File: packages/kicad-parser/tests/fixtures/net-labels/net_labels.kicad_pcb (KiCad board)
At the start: 4 copper layers, 40 x 40 mm, 2 parts, among them J1 NetLabels_Back, U1 NetLabels_Front

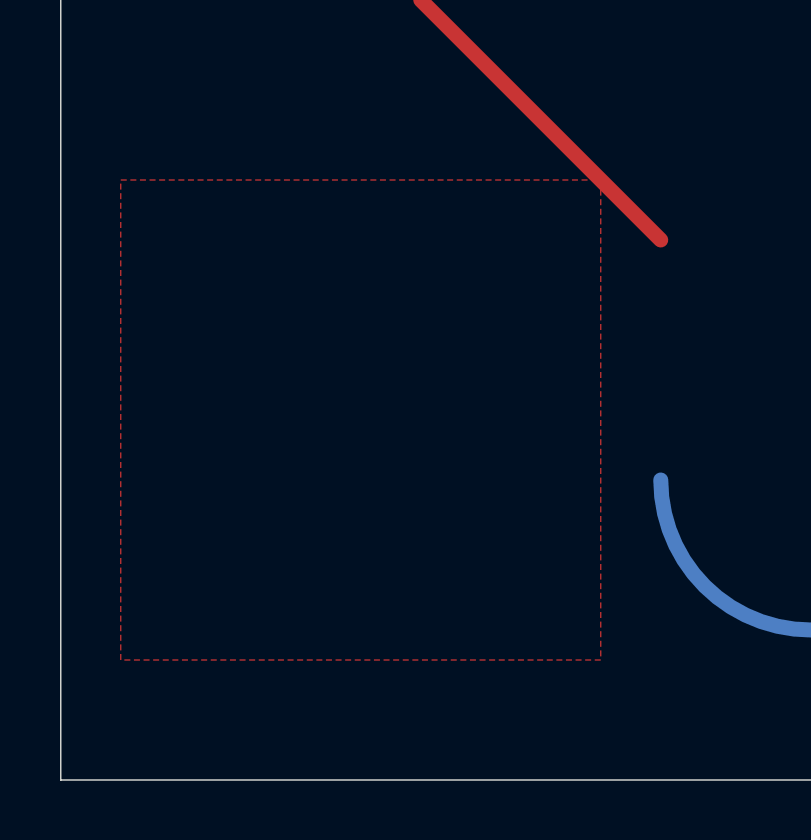
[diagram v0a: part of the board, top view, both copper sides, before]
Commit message: Revert "feat(board): net names inside filled zones"
This reverts commit d3646b39861fc9272b49cf270ddcd03324f96ff8.
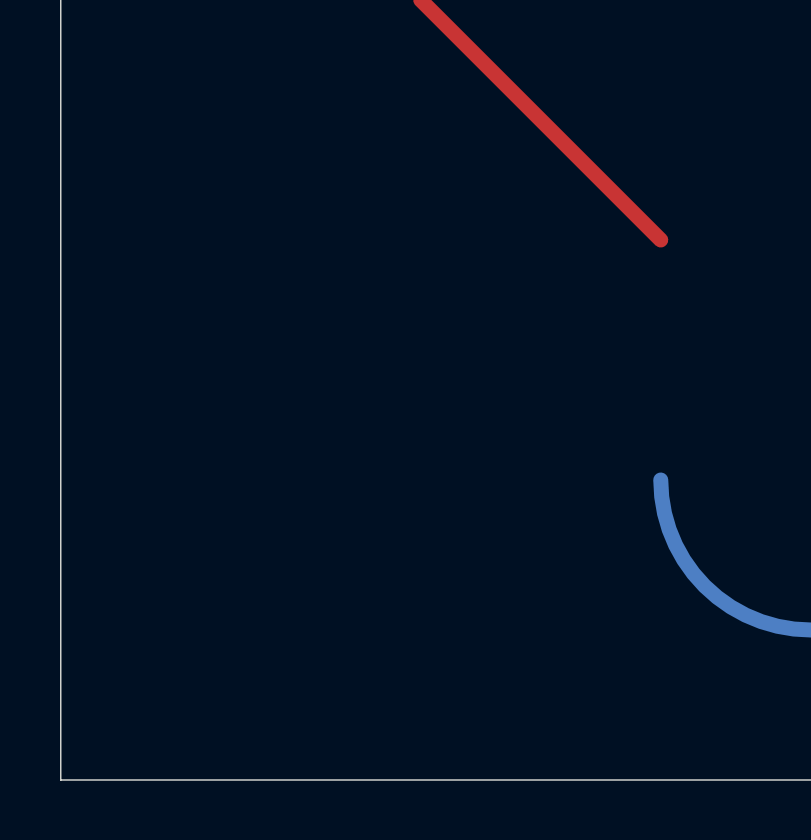
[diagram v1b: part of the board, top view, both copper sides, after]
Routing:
- removed copper zone on F.Cu, net GND
